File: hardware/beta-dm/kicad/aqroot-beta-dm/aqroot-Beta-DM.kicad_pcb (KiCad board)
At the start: 4 copper layers, 74 x 155 mm, 188 parts, among them J1 CH280QV10-CT_50P, J2 Molex_5025700893, J3 USB_C_Receptacle_USB2.0_16P, J4 JST-PH-2 BATTERY, J5 COMMUNITY_HEADER_2x13, J6 JST-PH-2 SPEAKER, Q1 AO3400A, SW1 BOOT, SW2 UP, SW3 DOWN, SW4 LEFT, SW5 RIGHT, SW6 A_SELECT, SW7 B_BACK, SW8 HOME, SW9 SW_SPDT, U1 ESP32-S3-WROOM-1, U10 USBLC6-2SC6, U11 BQ25185, U12 TPS63020, U13 TPS61023, U14 MAX17048, U15 TPS22918, U16 TCA9517ADGK, U17 TPS61169DCKR, U2 TCA9535PWR, U3 TCA9535PWR, U4 BMI270, U5 MAX98357A, U6 TSOP38238, U7 E07-400M10S, U8 E22-900M22S, U9 ST25R3916-AQET

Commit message: hardware(beta-dm): land the 4-object MCU release and the microphone-end R6
Copper. Only hardware/beta-dm/ is touched.

Four MCU-end release objects are removed and RE-LANDED - a release is not a
deletion, and every affected net stays one island:

  R1  /I2C_SDA_INT   In2  (17.500,37.000)-(17.500,10.875)  frees BCLK
      -> 27.798 mm, 2 vias, F.Cu + In2
  R2  /I2C_SCL_INT   B.Cu (10.030,36.000)-(18.200,36.000)  frees LRCLK
      -> 8.876 mm, 0 vias, B.Cu, as a 3-terminal tree
  R4  /BTN_RIGHT_N   In2  (24.701,35.985)-(23.300,33.481)  frees BOOT_N
      -> 3.304 mm, 0 vias, In2
  R5  /SPI_B_SCK     In2  (11.300,19.100)-(11.300,82.000)  frees FAST_IO
      -> 66.048 mm, 0 vias, In2

plus R6 at the microphone end: the three /SX1262_RXEN B.Cu segments move
0.200 mm south to y=11.000, which is what lets I2S_MIC_DIN out of the sealed
411-cell pocket at MK1.6.

LRCLK's release object is I2C_SCL_INT, NOT the BTN_RIGHT_N F.Cu stub the
earlier logical-role summary named, and the change is evidence-driven. With
BTN_RIGHT_N the SCL wall at y=36.000 stays, B.Cu is closed southward for
x 10.03-18.20, and all three I2S nets are forced onto F.Cu and In2 where the
northbound In2 lane under U1 has capacity one. Measured: six sequential orders
all fail after the first net, and negotiated congestion ran 32 iterations
without converging - best 12 conflict cells at iteration 22, oscillating.
Releasing the wall reopens B.Cu and the trio solves. It is still exactly four
objects, one per demand, with BTN_HOME excluded, which is the substance of the
ruling. The wall carries a T-junction at x=12.325 for the R20.2 tap, so its
re-land is a three-terminal tree rather than a two-point route.

The five DM fan-out via sites were reserved as hard obstacles BEFORE any
replacement was routed, so no re-land could steal one back. After landing, all
five demands are still escapable - FAST_IO 54 cells, BCLK 16, MIC_DIN 12,
BOOT_N 6, LRCLK 1 - and SPK_DOUT and IR_RX correctly remain at 0, which is the
chec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
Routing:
- net /SPI_B_SCK: track 210.6 -> 213.7 mm
- net /I2C_SDA_INT: track 168.9 -> 170.6 mm, vias 7 -> 9
- net /I2C_SCL_INT: track 178.9 -> 179.6 mm

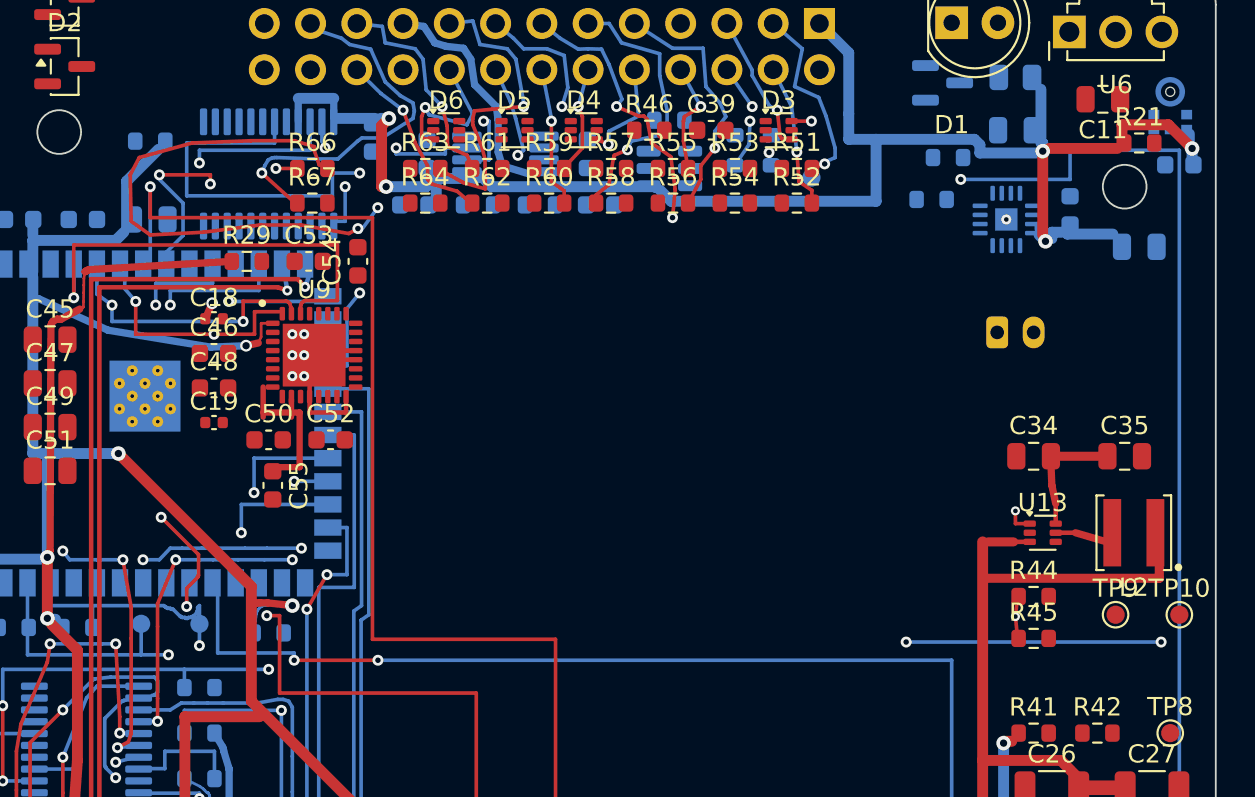
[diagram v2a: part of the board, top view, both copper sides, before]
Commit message: hardware(beta-dm): land the 3-net microphone I2S bus
Copper. Only hardware/beta-dm/ is touched.

  I2S_BCLK     U1.32 -> MK1.4   84.281 mm   5 vias   B.Cu 0.69  F.Cu 42.01  In2 41.58
  I2S_LRCLK    U1.33 -> MK1.1   87.909 mm   8 vias   B.Cu 41.33 F.Cu 19.30  In2 27.28
  I2S_MIC_DIN  U1.35 -> MK1.6   91.635 mm   8 vias   B.Cu 15.21 F.Cu 56.67  In2 19.75
  total                        263.824 mm  21 vias

Escape vias at (17.550,34.100), (16.700,35.550) and (13.650,35.000). There is no
I2S_SPK_DOUT demand on the Demo Model, so this is a 3-net problem and the paused
4-net Full-Beta conclusion was not reused.

The route is the artifact the previous pass solved by negotiated congestion and
validated, revalidated here against the CURRENT board with the final release
applied - 0 violations - with one net re-routed. BCLK had to move: the artifact
predates the BOOT_N and FAST_IO escape reservations and ran straight through
BOOT_N's escape window, leaving it 0 escape cells. Ripping up BCLK alone and
re-routing it with both sites held cost 0.030 mm and no extra via, and BOOT_N is
back to 6 cells.

Connectivity, from KiCad's own engine. I2S_MIC_DIN is ONE island holding U1.35
and MK1.6. I2S_BCLK and I2S_LRCLK are each two islands: the fitted circuit
(U1.32+MK1.4 and U1.33+MK1.1) and, separately, a single isolated pad - U5.16 and
U5.14. Those two are the DNP amplifier pins the ledger says not to route, so the
fitted DM circuit is one island per net and the two residual ratsnest lines are
correct forever on DM. Unconnected drops 281 -> 278, and the three lines that
closed are exactly the three U1-to-MK1 links.

DRC on the board with zones refilled: 0 errors, 240 warnings, and the warning
composition is unchanged from baseline including track_dangling still at 2.
Exact analytic validation of the full new copper set - 352 segments and 23 vias
across the I2S trio, the four re-lands and R6 - against every foreign pad
including custom-pad primitives, every track, every via on all four 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
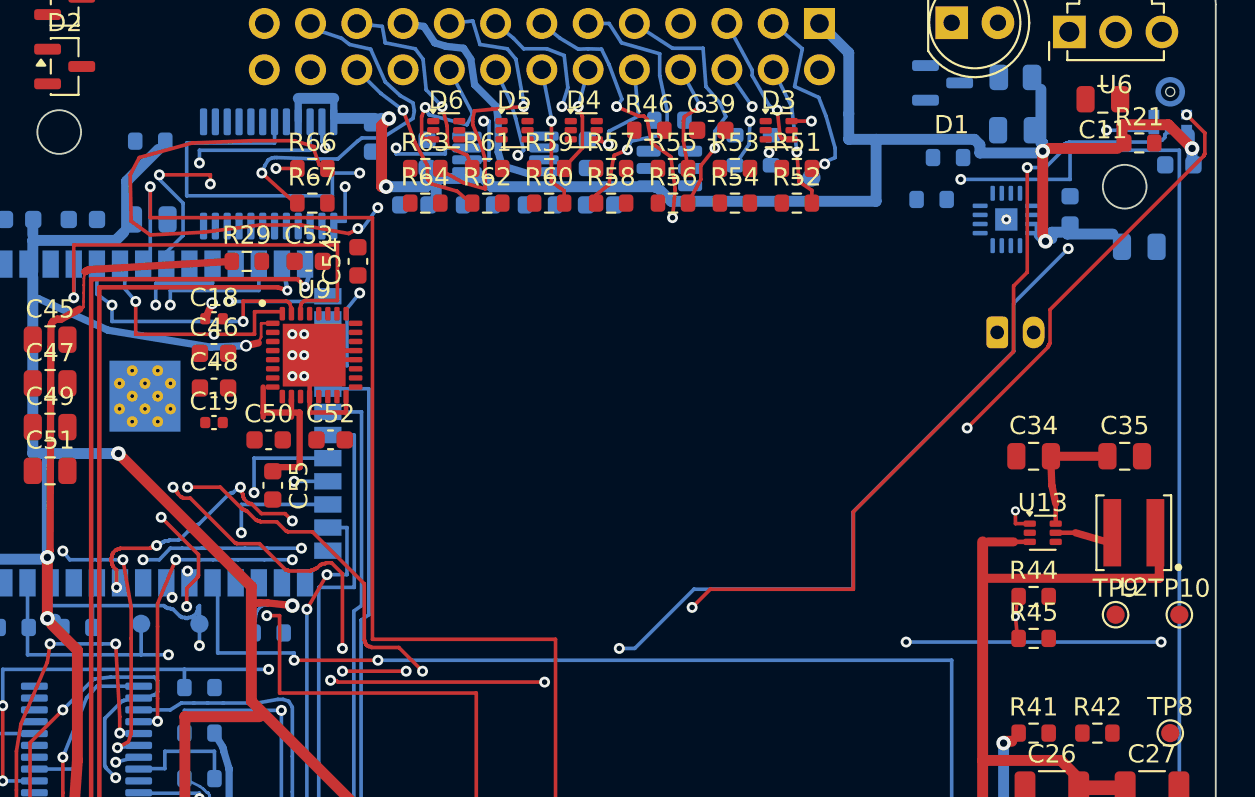
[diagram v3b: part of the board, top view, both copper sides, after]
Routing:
- net /I2S_MIC_DIN: track 0.00 -> 91.6 mm, vias 0 -> 8
- net /I2S_LRCLK: track 0.00 -> 87.9 mm, vias 0 -> 8
- net /I2S_BCLK: track 0.00 -> 84.3 mm, vias 0 -> 5

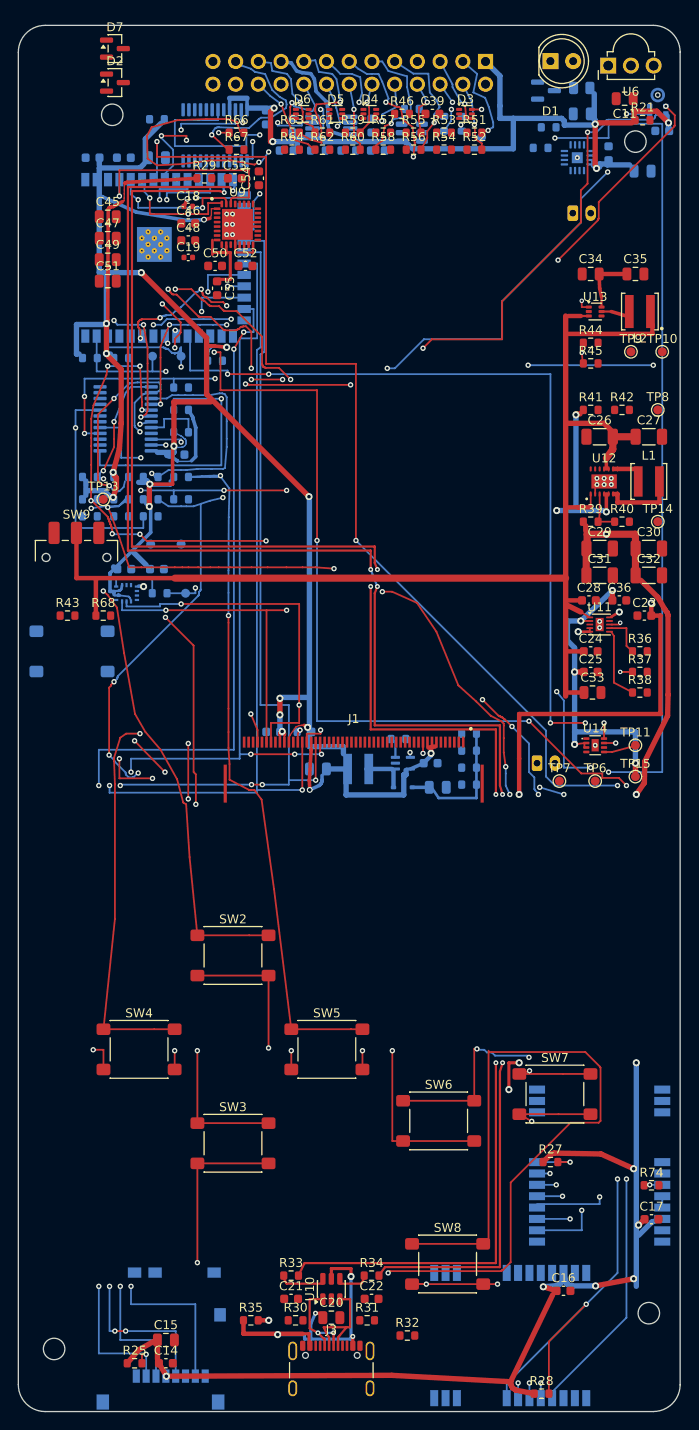
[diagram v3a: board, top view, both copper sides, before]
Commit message: hardware(beta-dm): FAST_IO, USB-C CC/shield and the critical power controls
Copper. Only hardware/beta-dm/ is touched. BOOT_N is NOT in this commit - it is
blocked by hard-locked copper and is returned for ruling rather than forced.

  /FAST_IO_U0TXD_ROOTPROBE_CS  U1.37 -> R67.2      99.603 mm  6 vias
  Net-(J3-CC1)                 J3.A5 -> R31.1      12.924 mm  0 vias
  Net-(J3-CC2)                 J3.B5 -> R30.1      15.707 mm  2 vias
  Net-(J3-SHIELD)              J3.SH x4 -> R32.1   21.054 mm  1 via
  Net-(U1-EN)                  U1.3 / R1.1 / C1.2   8.735 mm  2 vias
  Net-(U12-PS_SYNC)            U12.13 / R42.2 / TP14  22.828 mm  2 vias
  Net-(U12-PG)                 U12.14 / R41.2 / TP8   15.226 mm  2 vias
  Net-(U15-CT)                 U15.4 / C39.2       22.077 mm  1 via

USB-C topology audited from the schematic before routing, not assumed from net
names. J3 is a 16-pin USB 2.0 Type-C receptacle. CC1 (A5) goes to R31 and CC2
(B5) to R30, both 5.1 k to GND - the standard sink/UFP Rd termination, one per
CC line so BOTH cable orientations work, and neither resistor is DNP. The four
shield tabs go to R32, a 0 R link to GND: a deliberate placeable part so the tie
can become an RC network later, but as designed it is a hard DC connection, and
that is what was routed. SBU1/SBU2 are explicit no-connects, correct for USB
2.0. The two CC nets deliberately cross - CC1's resistor sits east of the
connector and CC2's west - which is why CC2 takes two vias.

Net-(U1-EN) is the ESP32-S3 reset RC (R1 10 k to +3V3, C1 1 uF to GND). It was
unrouted, which would have left the MCU's EN pin floating. Net-(U12-PS_SYNC)
ties the TPS63020 mode pin low through R42 (0 R); floating it leaves the
regulator's power-save behaviour undefined. Both are now closed.

Two model defects were found and fixed before anything landed, both caught by
KiCad disagreeing with the analytic check:

  * min_hole_clearance is a COPPER-to-HOLE rule on every layer, not just
    hole-to-hole. NPTH pads car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
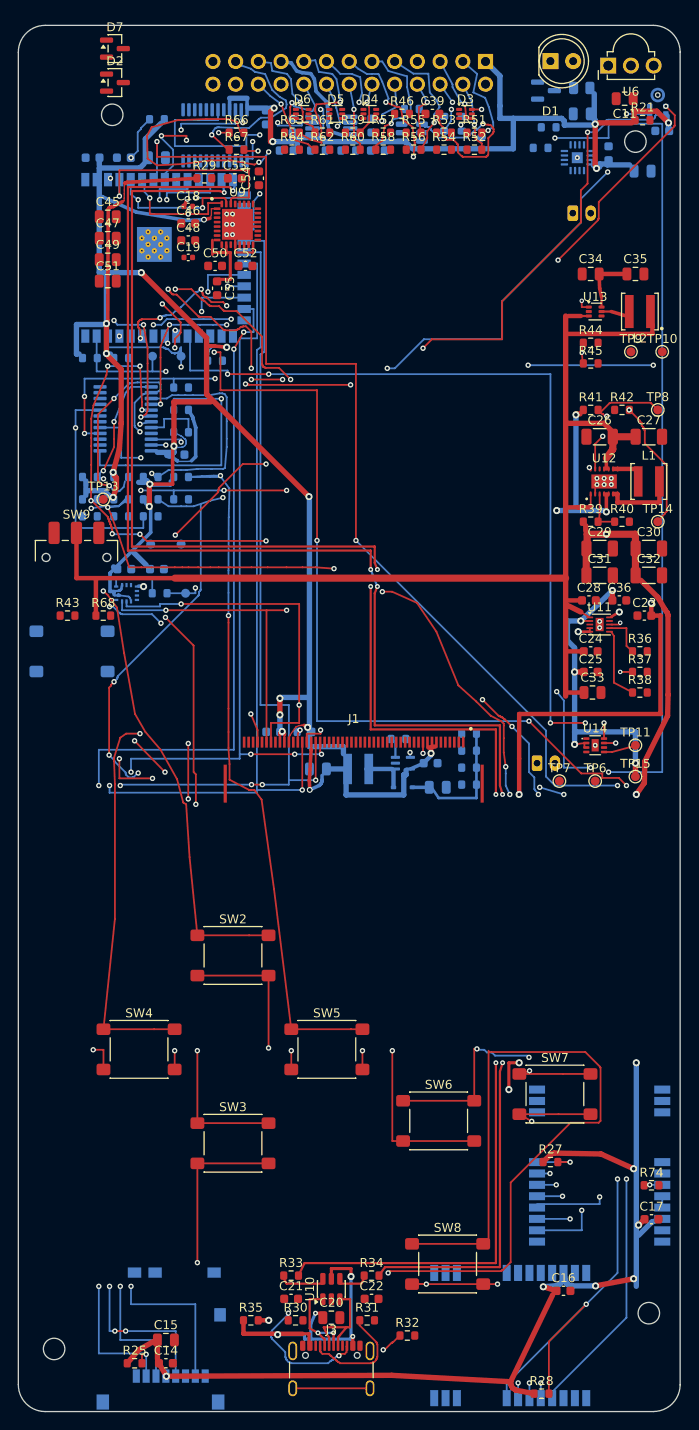
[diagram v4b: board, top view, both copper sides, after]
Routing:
- net /FAST_IO_U0TXD_ROOTPROBE_CS: track 0.00 -> 99.6 mm, vias 0 -> 6
- net Net-(U12-PS_SYNC): track 0.00 -> 22.8 mm, vias 0 -> 2
- net Net-(U15-CT): track 0.00 -> 22.1 mm, vias 0 -> 1
- net Net-(J3-SHIELD): track 0.00 -> 21.1 mm, vias 0 -> 1
- net Net-(J3-CC2): track 0.00 -> 15.7 mm, vias 0 -> 2
- net Net-(U12-PG): track 0.00 -> 15.2 mm, vias 0 -> 2
- net Net-(J3-CC1): track 0.00 -> 12.9 mm
- net Net-(U1-EN): track 0.00 -> 8.73 mm, vias 0 -> 2

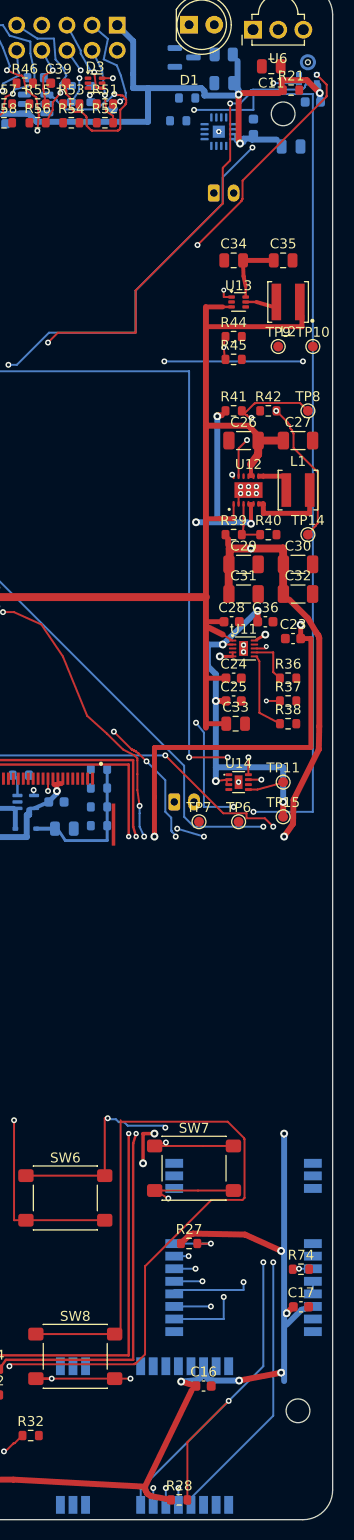
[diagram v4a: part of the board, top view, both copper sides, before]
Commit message: hardware(beta-dm): GND stitching for both radios and the microphone
Copper. Only hardware/beta-dm/ is touched. Pours are NOT in this commit - they
wait on BOOT_N, which is blocked and returned for ruling.

25 stitches: pad -> short stub -> via -> the In1 GND REFERENCE plane. This is
stitching, not GND routing: the plane is the return path, so each pad needs a
via into it rather than a trace across the board.

  U8  SX1262   10 pads  (1,2,3,4,5,10,11,12,20,22)
  U7  CC1101    9 pads  (1,2,3,4,5,11,12,20,22)
  MK1 mic       2 pads  (2,3)
  local decoupling returns: R74.2, C17.2, C16.2, C8.2

Stub lengths 0.536-1.074 mm, so every module ground pad has a short, local
return rather than a long detour. The CTO figures of 17/15/4 were ratsnest LINE
counts; recomputed from board geometry the distinct pad counts are 10/9/2, and
the four decoupling returns were added because a stitched module pad still drew
a ratsnest line to its un-stitched neighbouring capacitor.

No via was placed inside an RF band. The stitcher rejects any candidate inside
915 (y 88-114, full width) or 433 (x 0-52.5, y 115-138) before testing it, and
the landed vias sit at x 57.5-72.6 y 119-136 for U8 and y 139.5-154 for U7 -
outside both bands on both axes. The DRU forbids any via in band on any layer
and that is unchanged.

Result: GND ratsnest endpoints at U8 17 -> 0, U7 15 -> 0, MK1 4 -> 0, and
C8/C16/C17/R74 all 0. Board unconnected 264 -> 239.

Verification: exact analytic validation of 25 segments and 25 vias - 0
violations, minimum separation 0.200 mm, including the copper-to-hole check
against MK1's acoustic-port NPTH. Scratch replay with zones refilled: DRC 0
errors, 240 warnings, composition unchanged. Object-level preservation diff: 25
segments and 25 vias added, 0 changes to footprints, pads, zones or Edge.Cuts.
UUID prefix 7b31ef00, verified absent before writing.

BETA FULL DIRECTORY: UNCHANGED.

Co-Authored-By: Claude Opus 5 <noreply@anthropic.com>
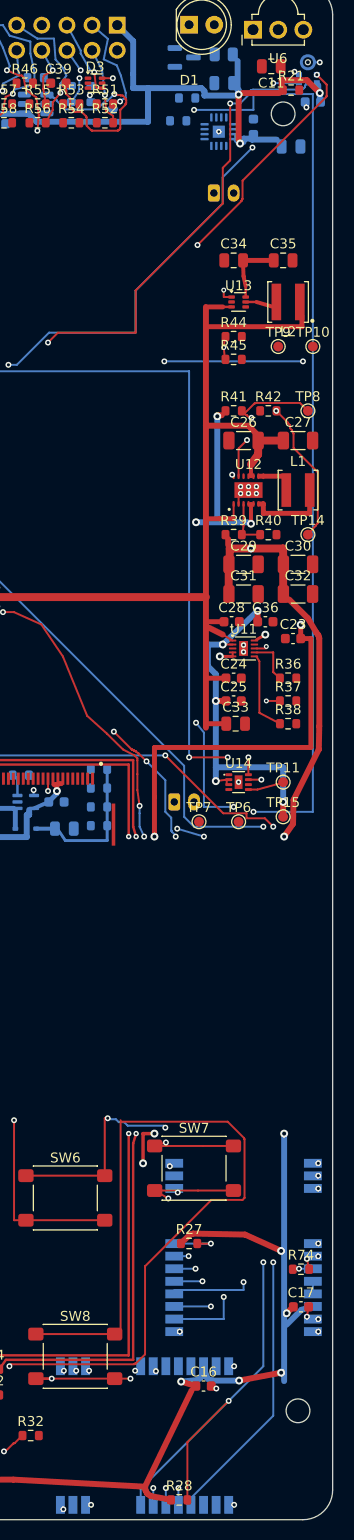
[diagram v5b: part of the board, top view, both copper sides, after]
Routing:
- net GND: track 91.9 -> 106.9 mm, vias 27 -> 52
